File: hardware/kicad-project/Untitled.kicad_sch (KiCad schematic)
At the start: 42 parts, among them CN2 ST-0322D00-071-1A2H, Q1 DMG2301L-7, Q2 DMG2301L-7, SW1 TS-1187A-B-A-B, SW2 TS-1187A-B-A-B, U1 ESP32-S3-WROOM-1-N8, U2 MCP73831-2ACI/MC, U4 XC6220B331MR, U6 MAX98357AETE+T

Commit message: add outputs
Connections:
- net GND: no longer CN2.1, H2.1, U6.10 (OUTN)
- new net: CN2.1, H2.1, U6.10 (OUTN)
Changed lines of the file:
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@@
   (junction (at 60.96 140.97) (diameter 0) (color 0 0 0 0)
-  )
-  (junction (at 173.99 77.47) (diameter 0) (color 0 0 0 0)
   )
   (junction (at 160.02 142.24) (diameter 0) (color 0 0 0 0)
@@
     (stroke (width 0) (type default))
   )
-  (wire (pts (xy 173.99 77.47) (xy 222.25 77.47))
+  (wire (pts (xy 171.45 77.47) (xy 222.25 77.47))
     (stroke (width 0) (type default))
   )
@@
     (stroke (width 0) (type default))
   )
-  (wire (pts (xy 171.45 77.47) (xy 173.99 77.47))
-    (stroke (width 0) (type default))
-  )
   (wire (pts (xy 205.74 59.69) (xy 238.76 59.69))
     (stroke (width 0) (type default))
@@
     (stroke (width 0) (type default))
   )
-  (wire (pts (xy 173.99 74.93) (xy 173.99 77.47))
-    (stroke (width 0) (type default))
-  )
   (wire (pts (xy 83.82 77.47) (xy 88.9 77.47))
     (stroke (width 0) (type default))
@@
     (stroke (width 0) (type default))
   )
-  (wire (pts (xy 173.99 77.47) (xy 173.99 85.09))
-    (stroke (width 0) (type default))
-  )
+  (wire (pts (xy 173.99 74.93) (xy 173.99 85.09))
+    (stroke (width 0) (type default))
+  )

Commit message: wip
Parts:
- removed R1, R11: 0, Resistor_SMD:R_0603_1608Metric, symbol Device:R
- added JP1: Gain jumper, Jumper:SolderJumper-2_P1.3mm_Open_Pad1.0x1.5mm, symbol Jumper:Jumper_2_Open
- added JP2: Power jumper, Jumper:SolderJumper-2_P1.3mm_Open_Pad1.0x1.5mm, symbol Jumper:Jumper_2_Open
- added TP1: Test OUTP, Connector_PinHeader_2.54mm:PinHeader_1x01_P2.54mm_Vertical, symbol Connector:TestPoint
- added TP2: Test OUTN, Connector_PinHeader_2.54mm:PinHeader_1x01_P2.54mm_Vertical, symbol Connector:TestPoint
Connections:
- net +3.3V: now also JP2.2 (B)
- net CONTROLLED_3.3V: now also JP2.1 (A)
- net GAIN_CONTROL: now also JP1.2 (B)
- net GND: now also JP1.1 (A)
- net SD_CLK: now also U1.34 (IO41); no longer U1.31 (IO38)
- net SD_CMD: now also U1.35 (IO42); no longer U1.32 (IO39)
- net SD_DAT_0: now also U1.33 (IO40); no longer U1.30 (IO37)
- net SD_DAT_1: now also U1.32 (IO39); no longer U1.29 (IO36)
- net SD_DAT_2: now also U1.39 (IO1); no longer U1.34 (IO41)
- net SD_DAT_3: now also U1.38 (IO2); no longer U1.33 (IO40)
- net at CN2.1, H2.1, U6.10 (OUTN): now also TP2.1
- net at CN2.2, CN2.3, CN2.4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: now also TP1.1
- net LCD_MOSI: now reaches U1.28 (IO35)
- new net LCD_CS: U1.31 (IO38)
- new net LCD_DC: U1.29 (IO36)
- new net LCD_SCK: U1.30 (IO37)

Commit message: update MAX sdmode to 634k R
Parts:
- R8: value 1M -> 634k
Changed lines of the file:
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@@
       (effects (font (size 1.27 1.27)) (justify left))
     )
-    (property "Value" "1M" (at 157.48 39.37 90)
+    (property "Value" "634k" (at 157.48 39.37 90)
       (effects (font (size 1.27 1.27)) (justify left))
     )

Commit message: fix mosfet
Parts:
- removed TP1: Test OUTP, Connector_PinHeader_2.54mm:PinHeader_1x01_P2.54mm_Vertical, symbol Connector:TestPoint
- removed TP2: Test OUTN, Connector_PinHeader_2.54mm:PinHeader_1x01_P2.54mm_Vertical, symbol Connector:TestPoint
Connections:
- net +3.3V: now also Q2.2 (S); no longer Q2.3 (D)
- net +BATT: now also Q1.2 (S); no longer Q1.3 (D)
- net CONTROLLED_3.3V: now also Q2.3 (D); no longer Q2.2 (S)
- net at C4.2, D1.1 (K), R4.2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: now also Q1.3 (D); no longer Q1.2 (S)
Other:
- moved on the sheet: Q1, Q2, R9

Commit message: wip
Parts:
- removed U4: XC6220B331MR, easyeda2kicad:SOT-23-5_L2.9-W1.6-P0.95-LS2.8-BR, symbol easyedaToKicad:XC6220B331MR
- added C12: 10uf, Capacitor_SMD:C_0603_1608Metric, symbol Device:C
- added U3: ME6217C33P5G, easyeda2kicad:SOT-89-5_L4.5-W2.5-P1.50-LS4.5-BR, symbol easyedaToKicad:ME6217C33P5G
- C4: value 10uF -> 10uf
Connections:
- net +3.3V: now also C12.2, U3.5 (VOUT); no longer C3.1
- net GND: now also C3.1, C12.1, U3.2 (VSS); no longer C3.2
- net at C4.2, D1.1 (K), Q1.3 (D)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: now also C3.2, U3.1 (CE), U3.4 (VIN)
- no-connect marks 7 -> 6
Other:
- moved on the sheet: C5, H1, R4, R5

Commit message: wip
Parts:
- removed JP1: Gain jumper, Jumper:SolderJumper-2_P1.3mm_Open_Pad1.0x1.5mm, symbol Jumper:Jumper_2_Open
- removed JP2: Power jumper, Jumper:SolderJumper-2_P1.3mm_Open_Pad1.0x1.5mm, symbol Jumper:Jumper_2_Open
- removed Q2: DMG2301L-7, easyeda2kicad:SOT-23-3_L2.9-W1.3-P1.90-LS2.4-BR, symbol easyedaToKicad:DMG2301L-7
- removed R10: 100k, Resistor_SMD:R_0603_1608Metric, symbol Device:R
- removed R8: 634k, Resistor_SMD:R_0603_1608Metric, symbol Device:R
- removed R9: 330, Resistor_SMD:R_0603_1608Metric, symbol Device:R
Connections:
- net CONTROLLED_3.3V is gone; now on net +3.3V: C7.2, C8.2, R6.1, U6.7 (VDD), U6.8 (VDD)
- net AMP_EN: now reaches U1.8 (IO15)
- net AMP_EN: now also U6.4 (~{SD_MODE})
- net PERIPH_EN: no longer names the net of U1.22 (IO14)
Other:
- note removed: "Peripherals power control LCD + SD + MAX"
- moved on the sheet: C7, C8

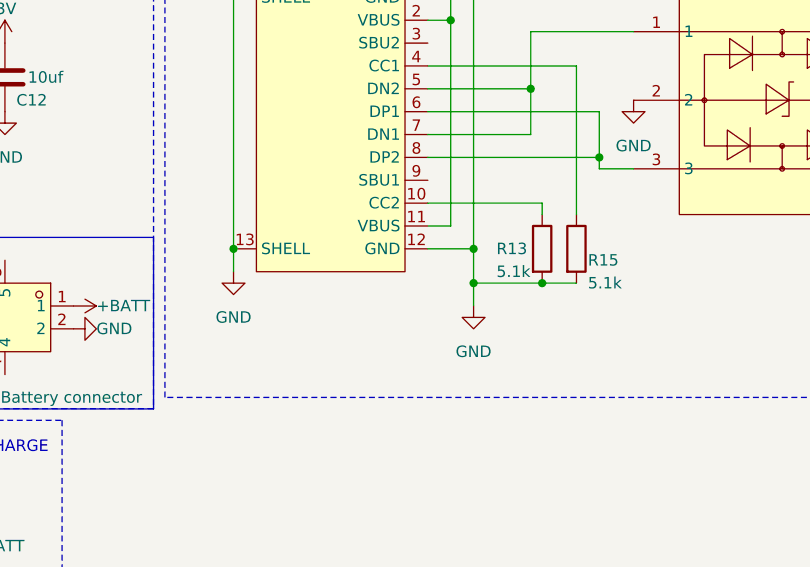
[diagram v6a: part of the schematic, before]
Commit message: New side buttons
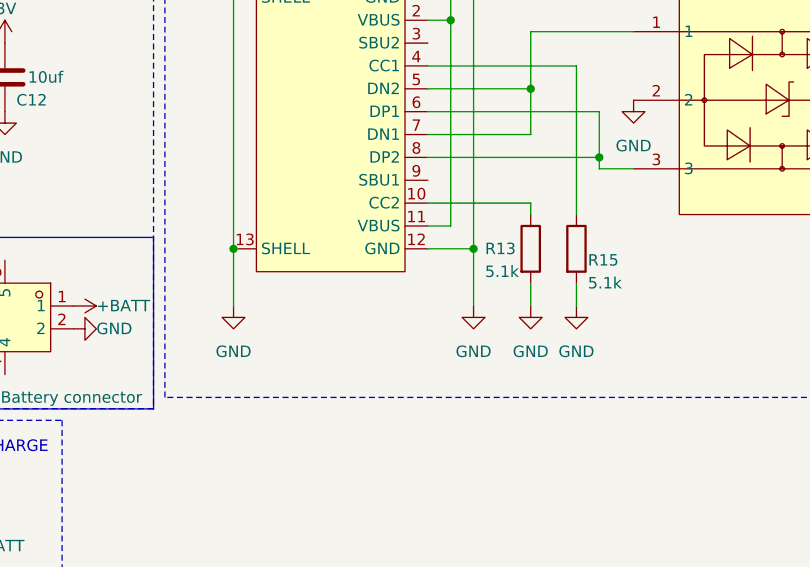
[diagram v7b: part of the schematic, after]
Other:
- moved on the sheet: R13
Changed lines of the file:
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@@
   (junction (at 34.29 134.62) (diameter 0) (color 0 0 0 0)
   )
-  (junction (at 160.02 142.24) (diameter 0) (color 0 0 0 0)
-  )
   (junction (at 252.73 107.95) (diameter 0) (color 0 0 0 0)
   )
@@
   )
   (junction (at 41.91 140.97) (diameter 0) (color 0 0 0 0)
-  )
-  (junction (at 152.4 142.24) (diameter 0) (color 0 0 0 0)
   )
   (junction (at 62.23 137.16) (diameter 0) (color 0 0 0 0)
@@
   (no_connect (at 76.2 83.82))
   (no_connect (at 245.11 125.73))
+  (wire (pts (xy 158.75 142.24) (xy 158.75 144.78))
+    (stroke (width 0) (type default))
+  )
   (wire (pts (xy 100.33 77.47) (xy 100.33 39.37))
     (stroke (width 0) (type default))
@@
     (stroke (width 0) (type default))
   )
-  (wire (pts (xy 160.02 133.35) (xy 160.02 134.62))
+  (wire (pts (xy 158.75 133.35) (xy 158.75 134.62))
     (stroke (width 0) (type default))
   )
@@
     (stroke (width 0) (type default))
   )
+  (wire (pts (xy 163.83 144.78) (xy 163.83 142.24))
+    (stroke (width 0) (type default))
+  )
   (wire (pts (xy 19.05 127) (xy 19.05 134.62))
     (stroke (width 0) (type default))
@@
     (stroke (width 0) (type default))
   )
-  (wire (pts (xy 152.4 142.24) (xy 152.4 144.78))
+  (wire (pts (xy 152.4 138.43) (xy 152.4 144.78))
     (stroke (width 0) (type default))
   )
@@
     (stroke (width 0) (type default))
   )
-  (wire (pts (xy 125.73 138.43) (xy 125.73 140.97))
+  (wire (pts (xy 125.73 138.43) (xy 125.73 144.78))
     (stroke (width 0) (type default))
   )
@@
     (stroke (width 0) (type default))
   )
-  (wire (pts (xy 147.32 133.35) (xy 160.02 133.35))
+  (wire (pts (xy 147.32 133.35) (xy 158.75 133.35))
     (stroke (width 0) (type default))
   )
@@
     (stroke (width 0) (type default))
   )
-  (wire (pts (xy 152.4 142.24) (xy 160.02 142.24))
-    (stroke (width 0) (type default))
-  )
   (wire (pts (xy 62.23 127) (xy 66.04 127))
     (stroke (width 0) (type default))
@@
     (stroke (width 0) (type default))
   )
-  (wire (pts (xy 152.4 138.43) (xy 152.4 142.24))
-    (stroke (width 0) (type default))
-  )
   (wire (pts (xy 57.15 115.57) (xy 57.15 121.92))
     (stroke (width 0) (type default))
@@
   )
   (wire (pts (xy 93.98 124.46) (xy 93.98 147.32))
-    (stroke (width 0) (type default))
-  )
-  (wire (pts (xy 160.02 142.24) (xy 163.83 142.24))
     (stroke (width 0) (type default))
   )
@@
         (path "/0de5ae84-7f75-4a5a-83a1-35d27fd1d8d2"
           (reference "#PWR02") (unit 1)
+        )
+      )
+    )
+  )
+  (symbol (lib_id "power:GND") (at 163.83 144.78 0) (unit 1)
+    (in_bom yes) (on_board yes) (dnp no) (fields_autoplaced)
+    (property "Reference" "#PWR044" (at 163.83 151.13 0)
+      (effects (font (size 1.27 1.27)) hide)
+    )
+    (property "Value" "GND" (at 163.83 149.86 0)
+      (effects (font (size 1.27 1.27)))
+    )
+    (property "Footprint" "" (at 163.83 144.78 0)
+      (effects (font (size 1.27 1.27)) hide)
+    )
+    (property "Datasheet" "" (at 163.83 144.78 0)
+      (effects (font (size 1.27 1.27)) hide)
+    )
+    (pin "1")
+    (instances
+      (project "Untitled"
+        (path "/0de5ae84-7f75-4a5a-83a1-35d27fd1d8d2"
+          (reference "#PWR044") (unit 1)
         )
       )
@@
     )
   )
-  (symbol (lib_id "Device:R") (at 160.02 138.43 0) (unit 1)
-    (in_bom yes) (on_board yes) (dnp no)
-    (property "Reference" "R13" (at 154.94 138.43 0)
-      (effects (font (size 1.27 1.27)) (justify left))
-    )
-    (property "Value" "5.1k" (at 154.94 140.97 0)
-      (effects (font (size 1.27 1.27)) (justify left))
-    )
-    (property "Footprint" "Resistor_SMD:R_0603_1608Metric" (at 158.242 138.43 90)
-      (effects (font (size 1.27 1.27)) hide)
-    )
-    (property "Datasheet" "~" (at 160.02 138.43 0)
+  (symbol (lib_id "Device:R") (at 158.75 138.43 0) (unit 1)
+    (in_bom yes) (on_board yes) (dnp no)
+    (property "Reference" "R13" (at 153.67 138.43 0)
+      (effects (font (size 1.27 1.27)) (justify left))
+    )
+    (property "Value" "5.1k" (at 153.67 140.97 0)
+      (effects (font (size 1.27 1.27)) (justify left))
+    )
+    (property "Footprint" "Resistor_SMD:R_0603_1608Metric" (at 156.972 138.43 90)
+      (effects (font (size 1.27 1.27)) hide)
+    )
+    (property "Datasheet" "~" (at 158.75 138.43 0)
       (effects (font (size 1.27 1.27)) hide)
     )
@@
     )
   )
-  (symbol (lib_id "power:GND") (at 125.73 140.97 0) (unit 1)
-    (in_bom yes) (on_board yes) (dnp no) (fields_autoplaced)
-    (property "Reference" "#PWR023" (at 125.73 147.32 0)
-      (effects (font (size 1.27 1.27)) hide)
-    )
-    (property "Value" "GND" (at 125.73 146.05 0)
-      (effects (font (size 1.27 1.27)))
-    )
-    (property "Footprint" "" (at 125.73 140.97 0)
-      (effects (font (size 1.27 1.27)) hide)
-    )
-    (property "Datasheet" "" (at 125.73 140.97 0)
+  (symbol (lib_id "power:GND") (at 125.73 144.78 0) (unit 1)
+    (in_bom yes) (on_board yes) (dnp no) (fields_autoplaced)
+    (property "Reference" "#PWR023" (at 125.73 151.13 0)
+      (effects (font (size 1.27 1.27)) hide)
+    )
+    (property "Value" "GND" (at 125.73 149.86 0)
+      (effects (font (size 1.27 1.27)))
+    )
+    (property "Footprint" "" (at 125.73 144.78 0)
+      (effects (font (size 1.27 1.27)) hide)
+    )
+    (property "Datasheet" "" (at 125.73 144.78 0)
       (effects (font (size 1.27 1.27)) hide)
     )
@@
         )
       )
+    )
+  )
+  (symbol (lib_id "power:GND") (at 158.75 144.78 0) (unit 1)
+    (in_bom yes) (on_board yes) (dnp no) (fields_autoplaced)
+    (property "Reference" "#PWR045" (at 158.75 151.13 0)
+      (effects (font (size 1.27 1.27)) hide)
+    )
+    (property "Value" "GND" (at 158.75 149.86 0)
+      (effects (font (size 1.27 1.27)))
+    )
+    (property "Footprint" "" (at 158.75 144.78 0)
+      (effects (font (size 1.27 1.27)) hide)
+    )
+    (property "Datasheet" "" (at 158.75 144.78 0)
+      (effects (font (size 1.27 1.27)) hide)
+    )
+    (pin "1")
+    (instances
+      (project "Untitled"
+        (path "/0de5ae84-7f75-4a5a-83a1-35d27fd1d8d2"
+          (reference "#PWR045") (unit 1)
+        )
+      )

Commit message: wip
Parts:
- renumbered SW2 to SW10, SW1 to SW9
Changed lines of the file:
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@@
   (symbol (lib_id "easyedaToKicad:TS-1187A-B-A-B") (at 267.97 110.49 0) (unit 1)
     (in_bom yes) (on_board yes) (dnp no) (fields_autoplaced)
-    (property "Reference" "SW1" (at 267.97 102.87 0)
+    (property "Reference" "SW9" (at 267.97 102.87 0)
       (effects (font (size 1.27 1.27)))
     )
@@
       (project "Untitled"
         (path "/0de5ae84-7f75-4a5a-83a1-35d27fd1d8d2"
-          (reference "SW1") (unit 1)
+          (reference "SW9") (unit 1)
         )
       )
@@
   (symbol (lib_id "easyedaToKicad:TS-1187A-B-A-B") (at 240.03 128.27 0) (unit 1)
     (in_bom yes) (on_board yes) (dnp no) (fields_autoplaced)
-    (property "Reference" "SW2" (at 240.03 120.65 0)
+    (property "Reference" "SW10" (at 240.03 120.65 0)
       (effects (font (size 1.27 1.27)))
     )
@@
       (project "Untitled"
         (path "/0de5ae84-7f75-4a5a-83a1-35d27fd1d8d2"
-          (reference "SW2") (unit 1)
-        )
-      )
+          (reference "SW10") (unit 1)
+        )
+      )
